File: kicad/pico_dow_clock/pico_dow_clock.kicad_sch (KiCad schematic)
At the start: 0 parts

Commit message: Updated schematic for bare LCDs
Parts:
- added A2: RaspberryPi_Pico, Module:RaspberryPi_Pico_SMD, symbol MCU_Module:RaspberryPi_Pico_Extensive
- added C1, C10, C11, C12, C13, C14, C2, C3, C4, C5, C6, C7, C8, C9: 10u, symbol Device:C
- added Q2: AO3400A, Package_TO_SOT_SMD:SOT-23, symbol Transistor_FET:AO3400A
- added R10, R11, R5, R6, R7, R8, R9: 15, symbol Device:R
- added R3: 10k, symbol Device:R
- added SW1: SW_Push_Dual, symbol Switch:SW_Push_Dual
- added U1: AMS1117-3.3, Package_TO_SOT_SMD:SOT-223-3_TabPin2, symbol Regulator_Linear:AMS1117-3.3
- added U10, U11, U12, U13, U7, U8, U9: LCD_ST7789, symbol Display_Graphic:LCD_ST7789
- added U4: SN74LVC245N, Package_SO:TSSOP-20_4.4x6.5mm_P0.65mm, symbol Logic_LevelTranslator:SN74LVC245APW
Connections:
- new net: C6.1, U9.2 (GND)
- new net: R11.2, U13.6 (LED-)
- new net: C9.2, U11.1 (VCC)
- new net: C10.1, U11.2 (GND)
- new net: R9.2, U11.6 (LED-)
- new net: C7.2, U10.1 (VCC)
- new net: R7.2, U9.6 (LED-)
- new net: C3.2, U8.1 (VCC)
- new net: C4.1, U8.2 (GND)
- new net: R6.2, U8.6 (LED-)
- new net: C8.1, U10.2 (GND)
- new net: R8.2, U10.6 (LED-)
- new net: C2.2, U7.1 (VCC)
- new net: C1.1, U7.2 (GND)
- new net: R5.2, U7.6 (LED-)
- new net: C12.1, U12.2 (GND)
- new net: C5.2, U9.1 (VCC)
- new net: C13.2, U13.1 (VCC)
- new net: R10.2, U12.6 (LED-)
- new net: C11.2, U12.1 (VCC)
- new net: C14.1, U13.2 (GND)
- new net +3.3V: C11.1, C13.1, C2.1, C3.1, C5.1, C7.1, C9.1, U1.2 (VO), U10.5 (LED+), U11.5 (LED+), U12.5 (LED+), U13.5 (LED+), U4.1 (DIR), U4.20 (VCC), U7.5 (LED+), U8.5 (LED+), U9.5 (LED+)
- new net +5V: A2.39 (VSYS), U1.3 (VI)
- new net BL_POWER: Q2.3 (D), R11.1, R8.1
- new net FACT_RESET: A2.12 (GPIO9), SW1.1
- new net GND: A2.13 (GND), A2.18 (GND), A2.23 (GND), A2.28 (GND), A2.3 (GND), A2.38 (GND), A2.8 (GND), A2.D2 (GND), C1.2, C10.2, C12.2, C14.2, C4.2, C6.2, C8.2, Q2.2 (S), R3.2, SW1.2, U1.1 (GND), U4.10 (GND), U4.19 (~{OE}), U4.6 (A5), U4.7 (A6), U4.8 (A7), U4.9 (A8)
- new net LCD_1_CS: A2.4 (GPIO2), U10.7 (CS), U11.7 (CS), U12.7 (CS), U13.7 (CS), U7.7 (CS), U8.7 (CS), U9.7 (CS)
- new net LCD_2_CS: A2.5 (GPIO3)
- new net LCD_3_CS: A2.6 (GPIO4)
- new net LCD_4_CS: A2.7 (GPIO5)
- new net LCD_5_CS: A2.9 (GPIO6)
- new net LCD_6_CS: A2.10 (GPIO7)
- new net LCD_7_CS: A2.11 (GPIO8)
- new net LCD_BL: Q2.1 (G), R3.1
- new net LCD_CLK: U10.4 (CLK), U11.4 (CLK), U12.4 (CLK), U13.4 (CLK), U4.16 (B3), U7.4 (CLK), U8.4 (CLK), U9.4 (CLK)
- new net LCD_DC: U10.9 (DC), U11.9 (DC), U12.9 (DC), U13.9 (DC), U4.15 (B4), U7.9 (DC), U8.9 (DC), U9.9 (DC)
- new net LCD_DIN: U10.3 (DIN), U11.3 (DIN), U12.3 (DIN), U13.3 (DIN), U4.17 (B2), U7.3 (DIN), U8.3 (DIN), U9.3 (DIN)
- new net LCD_RST: U10.8 (RST), U11.8 (RST), U12.8 (RST), U13.8 (RST), U4.18 (B1), U7.8 (RST), U8.8 (RST), U9.8 (RST)
- new net P_LCD_BL: A2.17 (GPIO13)
- new net P_LCD_CLK: A2.14 (GPIO10), U4.4 (A3)
- new net P_LCD_DC: A2.19 (GPIO14), U4.5 (A4)
- new net P_LCD_DIN: A2.15 (GPIO11), U4.3 (A2)
- new net P_LCD_RST: A2.16 (GPIO12), U4.2 (A1)
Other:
- note added: "Backlight Control"
- note added: "Factory Reset"
- note added: "LCD Circuits"
- note added: "LCD Driver"
- note added: "Power Supply"
- note added: "Raspberry Pi Pico 2W"
- title: (none) -> Raspberry Pi Pico Day of Week Clock

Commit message: Rev0 schematic
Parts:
- added J1: (no value), USB C Vertical:USB-C-8P-2LAYER-VERTICAL-PTH, symbol Connector:USB_C_2-LAYER-VERTICAL-PTH
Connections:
- net P_LCD_BL is gone; now on net LCD_BL: A2.17 (GPIO13)
- net BL_POWER: now also R10.1, R5.1, R6.1, R7.1, R9.1
- net GND: now also A2.TP1 (USB_GND), J1.A1 (GND), J1.A12 (GND), J1.B1 (GND), J1.B12 (GND), J1.SHLD1 (SHLD), J1.SHLD2 (SHLD), J1.SHLD3 (SHLD), J1.SHLD4 (SHLD)
- net LCD_1_CS: no longer U10.7 (CS), U11.7 (CS), U12.7 (CS), U13.7 (CS), U8.7 (CS), U9.7 (CS)
- net LCD_2_CS: now also U8.7 (CS)
- net LCD_3_CS: now also U9.7 (CS)
- net LCD_4_CS: now also U10.7 (CS)
- net LCD_5_CS: now also U11.7 (CS)
- net LCD_6_CS: now also U12.7 (CS)
- net LCD_7_CS: now also U13.7 (CS)
- net VBUS: now reaches A2.40 (VBUS)
- net VBUS: now also J1.A4 (VBUS), J1.A9 (VBUS), J1.B4 (VBUS), J1.B9 (VBUS)
- net USB-D-: now reaches A2.TP2 (USB_DM)
- net USB-D-: now also J1.A6 (D+), J1.B6 (D+)
- net USB-D+: now reaches A2.TP3 (USB_DP)
- net USB-D+: now also J1.A7 (D-), J1.B7 (D-)
- no-connect marks 0 -> 31
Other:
- note added: "Backlight"
- note added: "USB"
- note removed: "Backlight Control"
- moved on the sheet: A2, C2, C3, C5, R5, R6, R7, SW1, U1, U7, U8, U9

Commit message: Rev 0.1 of schematic with no ERC errors/warnings
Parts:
- removed C10, C11, C12, C13, C14, C8, C9: 10u, symbol Device:C
- removed J1: (no value), USB C Vertical:USB-C-8P-2LAYER-VERTICAL-PTH, symbol Connector:USB_C_2-LAYER-VERTICAL-PTH
- removed R10, R11, R5, R6, R7, R8, R9: 15, symbol Device:R
- removed U10, U11, U12, U13, U7, U8, U9: LCD_ST7789, symbol Display_Graphic:LCD_ST7789
- added LCD1, LCD2, LCD3, LCD4, LCD5, LCD6, LCD7: LCD_ST7789, symbol local_symbols:LCD_ST7789
- added R1: 10k, symbol Device:R
- added R12, R13, R14, R15, R16, R17, R18: 15, symbol Device:R
- added USB1: Sparkfun_BOB_23055, symbol local_symbols:Sparkfun_BOB_23055
- C1, C2, C3, C4, C5, C6, C7: value 10u -> 0.1u
- CPU1: renamed from A2; footprint Module:RaspberryPi_Pico_SMD -> Module_RaspberryPi_Pico:RaspberryPi_Pico_Original_SMD; symbol MCU_Module:RaspberryPi_Pico_Extensive -> local_symbols:RaspberryPi_Pico_SecondaryPins
- renumbered U4 to LEV1
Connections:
- net +3.3V: now also C1.1, C4.1, C6.1, LCD1.1 (VCC), LCD1.5 (LED+), LCD2.1 (VCC), LCD2.5 (LED+), LCD3.1 (VCC), LCD3.5 (LED+), LCD4.1 (VCC), LCD4.5 (LED+), LCD5.1 (VCC), LCD5.5 (LED+), LCD6.1 (VCC), LCD6.5 (LED+), LCD7.1 (VCC), LCD7.5 (LED+)
- net BL_POWER: now also R12.1, R13.1, R14.1, R15.1, R16.1, R17.1, R18.1
- net GND: now also C2.2, C3.2, C5.2, C7.2, LCD1.2 (GND), LCD2.2 (GND), LCD3.2 (GND), LCD4.2 (GND), LCD5.2 (GND), LCD6.2 (GND), LCD7.2 (GND), R1.2, USB1.6 (SHLD), USB1.7 (GND); no longer CPU1.13 (GND), CPU1.18 (GND), CPU1.23 (GND), CPU1.28 (GND), CPU1.3 (GND), CPU1.38 (GND), CPU1.8 (GND), CPU1.D2 (GND), LEV1.6 (A5), LEV1.7 (A6), LEV1.8 (A7), LEV1.9 (A8)
- net LCD_1_CS: now also LCD1.7 (CS)
- net LCD_2_CS: now also LCD2.7 (CS)
- net LCD_3_CS: now also LCD3.7 (CS)
- net LCD_4_CS: now also LCD4.7 (CS)
- net LCD_5_CS: now also LCD5.7 (CS)
- net LCD_6_CS: now also LCD6.7 (CS)
- net LCD_7_CS: now also LCD7.7 (CS)
- net LCD_CLK: now also LCD1.4 (CLK), LCD2.4 (CLK), LCD3.4 (CLK), LCD4.4 (CLK), LCD5.4 (CLK), LCD6.4 (CLK), LCD7.4 (CLK)
- net LCD_DC: now also LCD1.9 (DIN), LCD2.9 (DIN), LCD3.9 (DIN), LCD4.9 (DIN), LCD5.9 (DIN), LCD6.9 (DIN), LCD7.9 (DIN)
- net LCD_DIN: now also LCD1.3 (DIN), LCD2.3 (DIN), LCD3.3 (DIN), LCD4.3 (DIN), LCD5.3 (DIN), LCD6.3 (DIN), LCD7.3 (DIN)
- net LCD_RST: now also LCD1.8 (RST), LCD2.8 (RST), LCD3.8 (RST), LCD4.8 (RST), LCD5.8 (RST), LCD6.8 (RST), LCD7.8 (RST)
- net USB-D+: now also CPU1.TP2 (USB_DM), USB1.3 (D-); no longer CPU1.TP3 (USB_DP)
- net USB-D-: now also CPU1.TP3 (USB_DP), USB1.2 (D+); no longer CPU1.TP2 (USB_DM)
- net VBUS: now also U1.3 (VI), USB1.1 (VBUS)
- net +5V: no longer names the net of CPU1.39 (VSYS)
- net +5V: no longer U1.3 (VI)
- new net: LCD5.6 (LED-), R16.2
- new net: LCD7.6 (LED-), R18.2
- new net: LCD2.6 (LED-), R13.2
- new net: LCD3.6 (LED-), R14.2
- new net: LEV1.6 (A5), LEV1.7 (A6), LEV1.8 (A7), LEV1.9 (A8), R1.1
- new net: LCD1.6 (LED-), R12.2
- new net: CPU1.13 (GND), CPU1.18 (GND), CPU1.23 (GND), CPU1.28 (GND), CPU1.3 (GND), CPU1.38 (GND), CPU1.8 (GND), CPU1.D2 (GND)
- new net: LCD4.6 (LED-), R15.2
- new net: LCD6.6 (LED-), R17.2
- no-connect marks 31 -> 32
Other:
- note added: "LCD Power Rail Decoupling"
- moved on the sheet: Q2, R3, SW1, U1

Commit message: Added LED
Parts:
- added D1: LED, symbol Device:LED
- added R2: 325, symbol Device:R
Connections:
- net BL_POWER: no longer R18.1
- net GND: now also D1.1 (K)
- net LED: now reaches CPU1.20 (GPIO15)
- net LED: now also R2.1
- new net: D1.2 (A), R2.2
- no-connect marks 32 -> 31
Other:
- note added: "Diagnostic LED"
- company: (none) -> Contact: python@figsandfudge.com
- moved on the sheet: LCD4, LCD5, LCD6, LCD7, R15, R16, R17, R18

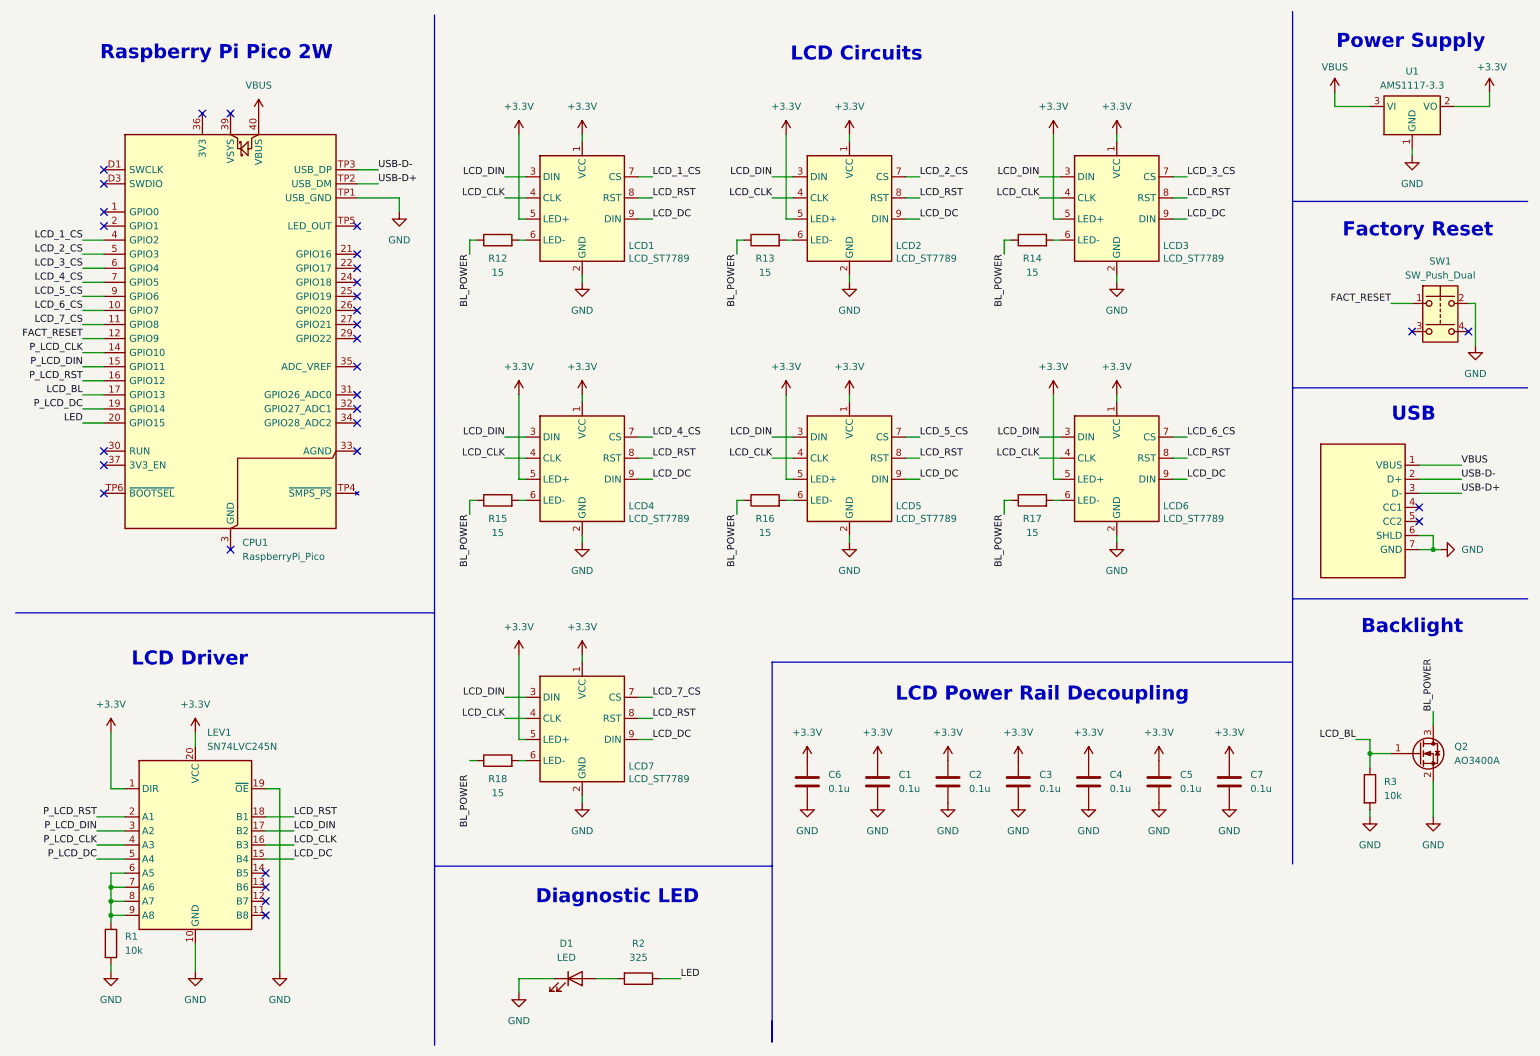
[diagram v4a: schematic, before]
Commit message: Use bidirectional red-green LED
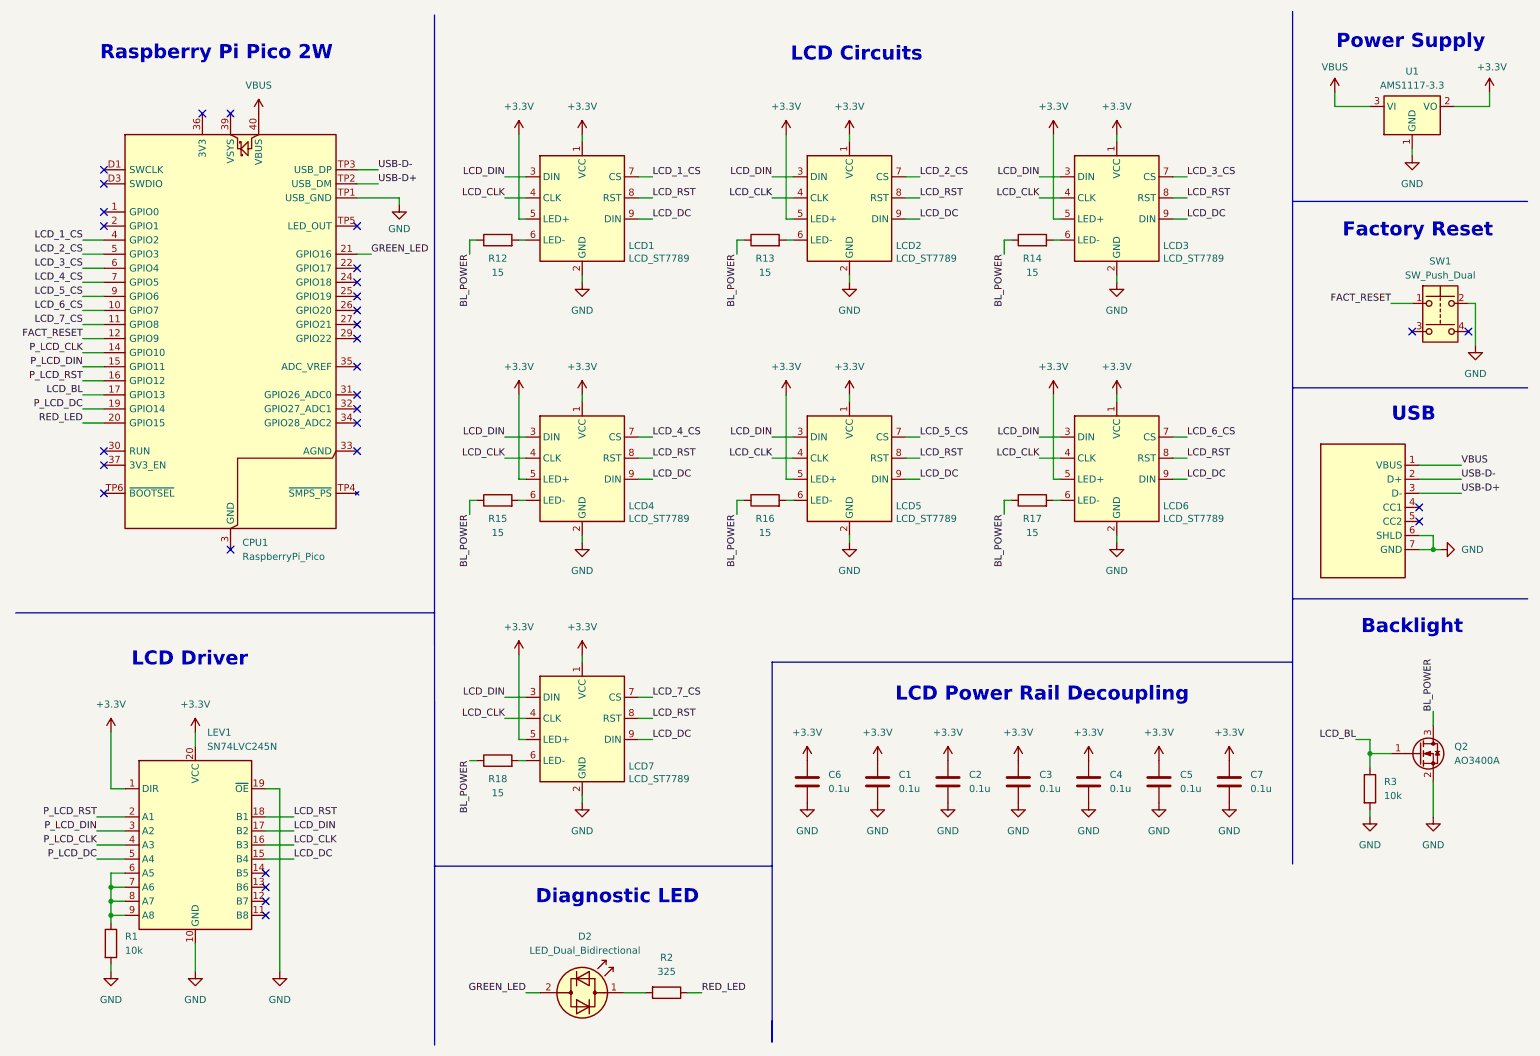
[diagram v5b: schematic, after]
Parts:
- removed D1: LED, symbol Device:LED
- added D2: LED_Dual_Bidirectional, symbol Device:LED_Dual_Bidirectional
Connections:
- net BL_POWER: now also R18.1
- net at R2.2: now also D2.1 (KA)
- net GREEN_LED: now reaches CPU1.21 (GPIO16)
- net GREEN_LED: now also D2.2 (AK)
- net LED renamed RED_LED
- no-connect marks 31 -> 30
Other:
- moved on the sheet: R2
